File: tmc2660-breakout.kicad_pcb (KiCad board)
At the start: 2 copper layers, 26.9 x 31.1 mm, 25 parts, among them P1 SPI, P2 StepDir, P3 Motor, P4 VCC, P5 VMOT, U1 TMC2660

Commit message: o smallish alignments
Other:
- board text added: "<30V"
- board text added: "I/O"
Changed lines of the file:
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@@
-(kicad_pcb (version 4) (host pcbnew "(2016-01-05 BZR 6425, Git 89c183f)-product")
+(kicad_pcb (version 20160815) (host pcbnew "(2016-10-23 revision 4ee344e)-master")
   (general
     (links 65)
     (no_connects 0)
-    (area 112.74 37.159999 147.476858 73.075952)
+    (area 112.9075 37.159999 156.503832 76.545001)
     (thickness 1.6)
-    (drawings 13)
-    (tracks 333)
+    (drawings 17)
+    (tracks 332)
     (zones 0)
     (modules 25)
@@
       (hpglpenspeed 20)
       (hpglpendiameter 15)
-      (hpglpenoverlay 2)
       (psnegative false)
       (psa4output false)
@@
     (uvia_dia 0.3)
     (uvia_drill 0.1)
+    (diff_pair_gap 0.25)
+    (diff_pair_width 0.2)
     (add_net /BRA)
     (add_net /BRB)
@@
     (tags "resistor 1206")
     (attr smd)
-    (fp_text reference R5 (at 0.039 0 360) (layer F.SilkS)
+    (fp_text reference R5 (at 0.039 0) (layer F.SilkS)
       (effects (font (size 1 1) (thickness 0.15)))
     )
@@
     (tags "capacitor 0805")
     (attr smd)
-    (fp_text reference C1 (at -1.778 -1.778 360) (layer F.SilkS)
+    (fp_text reference C1 (at -1.778 -1.778) (layer F.SilkS)
       (effects (font (size 1 1) (thickness 0.15)))
     )
@@
     (tags "capacitor 0805")
     (attr smd)
-    (fp_text reference C2 (at -1.143 -1.778 360) (layer F.SilkS)
+    (fp_text reference C2 (at -0.999 -1.68) (layer F.SilkS)
       (effects (font (size 1 1) (thickness 0.15)))
     )
@@
     (tags "LED 0805 SMD")
     (attr smd)
-    (fp_text reference D1 (at -2.286 0.635) (layer F.SilkS)
+    (fp_text reference D1 (at -2.621 0.266) (layer F.SilkS)
       (effects (font (size 1 1) (thickness 0.15)))
     )
@@
       (effects (font (size 1 1) (thickness 0.15)))
     )
-    (fp_text value SPI (at -2.54 4.445 360) (layer F.SilkS)
+    (fp_text value SPI (at -2.54 4.445) (layer F.SilkS)
       (effects (font (size 1.5 1.5) (thickness 0.2)))
     )
@@
       (effects (font (size 1 1) (thickness 0.15)))
     )
-    (fp_text value Motor (at -2.54 0.381 360) (layer F.SilkS)
+    (fp_text value Motor (at -2.54 0.381) (layer F.SilkS)
       (effects (font (size 1 1) (thickness 0.15)))
     )
@@
     (tags "resistor 0805")
     (attr smd)
-    (fp_text reference R2 (at -2.54 0.381 360) (layer F.SilkS)
+    (fp_text reference R2 (at -2.54 0.381) (layer F.SilkS)
       (effects (font (size 1 1) (thickness 0.15)))
     )
@@
     (tags "resistor 1206")
     (attr smd)
-    (fp_text reference R4 (at 0.039 0.0635 360) (layer F.SilkS)
+    (fp_text reference R4 (at 0.039 0.0635) (layer F.SilkS)
       (effects (font (size 1 1) (thickness 0.15)))
     )
@@
       (effects (font (size 1 1) (thickness 0.15)) (justify mirror))
     )
-    (fp_text value OSHW (at 4.445 -1.778 540) (layer B.Fab) hide
+    (fp_text value OSHW (at 4.445 -1.778 180) (layer B.Fab) hide
       (effects (font (size 1 1) (thickness 0.15)) (justify mirror))
     )
@@
     (fp_line (start 0.35052 -0.89916) (end 0.7493 -1.89992) (layer B.SilkS) (width 0.15))
   )
-  (module Fiducials:Fiducial_1mm_Dia_2.54mm_Outer_CopperTop (layer F.Cu)
+  (module Fiducials:Fiducial_1mm_Dia_2.54mm_Outer_CopperTop locked (layer F.Cu)
     (at 141.732 38.862)
     (descr "Circular Fiducial, 1mm bare copper top; 2.54mm keepout")
@@
       (solder_mask_margin 0.77) (clearance 0.77))
   )
-  (module Fiducials:Fiducial_1mm_Dia_2.54mm_Outer_CopperTop (layer F.Cu)
+  (module Fiducials:Fiducial_1mm_Dia_2.54mm_Outer_CopperTop locked (layer F.Cu)
     (at 118.11 66.548)
     (descr "Circular Fiducial, 1mm bare copper top; 2.54mm keepout")
@@
     (tags "resistor 2512")
     (attr smd)
-    (fp_text reference R6 (at 1.4605 0.0635 360) (layer F.SilkS)
+    (fp_text reference R6 (at 1.4605 0.0635) (layer F.SilkS)
       (effects (font (size 1 1) (thickness 0.15)))
     )
@@
     (tags "resistor 2512")
     (attr smd)
-    (fp_text reference R7 (at 1.5875 0 360) (layer F.SilkS)
-      (effects (font (size 1 1) (thickness 0.15)))
-    )
-    (fp_text value 0.075 (at -1.4605 -6.731 450) (layer F.Fab)
+    (fp_text reference R7 (at 1.5875 0) (layer F.SilkS)
+      (effects (font (size 1 1) (thickness 0.15)))
+    )
+    (fp_text value 0.075 (at -1.4605 -6.731 90) (layer F.Fab)
       (effects (font (size 1 1) (thickness 0.15)))
     )
@@
     (tags "capacitor 0805")
     (attr smd)
-    (fp_text reference C8 (at -0.889 -2.413 360) (layer F.SilkS)
-      (effects (font (size 1 1) (thickness 0.15)))
-    )
-    (fp_text value 10n (at 4.826 0 450) (layer F.Fab)
+    (fp_text reference C8 (at -0.889 -2.413) (layer F.SilkS)
+      (effects (font (size 1 1) (thickness 0.15)))
+    )
+    (fp_text value 10n (at 4.826 0 90) (layer F.Fab)
       (effects (font (size 1 1) (thickness 0.15)))
     )
@@
       (rotate (xyz 0 0 0))
     )
+  )
+  (dimension 27 (width 0.3) (layer Eco1.User)
+    (gr_text "27.000 mm" (at 129.5 75.15) (layer Eco1.User)
+      (effects (font (size 1.5 1.5) (thickness 0.3)))
+    )
+    (feature1 (pts (xy 143 69) (xy 143 76.5)))
+    (feature2 (pts (xy 116 69) (xy 116 76.5)))
+    (crossbar (pts (xy 116 73.8) (xy 143 73.8)))
+    (arrow1a (pts (xy 143 73.8) (xy 141.873496 74.386421)))
+    (arrow1b (pts (xy 143 73.8) (xy 141.873496 73.213579)))
+    (arrow2a (pts (xy 116 73.8) (xy 117.126504 74.386421)))
+    (arrow2b (pts (xy 116 73.8) (xy 117.126504 73.213579)))
+  )
+  (dimension 31.1 (width 0.3) (layer Eco1.User)
+    (gr_text "31.100 mm" (at 149.853831 53.15 270) (layer Eco1.User)
+      (effects (font (size 1.5 1.5) (thickness 0.3)))
+    )
+    (feature1 (pts (xy 143.3 68.7) (xy 151.203831 68.7)))
+    (feature2 (pts (xy 143.3 37.6) (xy 151.203831 37.6)))
+    (crossbar (pts (xy 148.503831 37.6) (xy 148.503831 68.7)))
+    (arrow1a (pts (xy 148.503831 68.7) (xy 147.91741 67.573496)))
+    (arrow1b (pts (xy 148.503831 68.7) (xy 149.090252 67.573496)))
+    (arrow2a (pts (xy 148.503831 37.6) (xy 147.91741 38.726504)))
+    (arrow2b (pts (xy 148.503831 37.6) (xy 149.090252 38.726504)))
+  )
+  (gr_text I/O (at 120.777 41.402) (layer F.SilkS)
+    (effects (font (size 0.8 0.8) (thickness 0.15)) (justify left))
+  )
+  (gr_text <30V (at 138.811 43.053) (layer F.SilkS)
+    (effects (font (size 0.8 0.8) (thickness 0.15)) (justify right))
   )
   (gr_text "github.com\nhzeller/tmc2660-breakout" (at 135.128 41.402 90) (layer B.SilkS)
@@
   (segment (start 124.696602 64.786) (end 123.571 64.786) (width 0.4) (layer F.Cu) (net 4))
   (segment (start 126.6575 60.206) (end 126.6575 62.825102) (width 0.4) (layer F.Cu) (net 4))
-  (segment (start 122.2375 52.756) (end 121.464 52.756) (width 0.5) (layer F.Cu) (net 5))
-  (segment (start 124.0075 52.756) (end 122.2375 52.756) (width 0.5) (layer F.Cu) (net 5))
-  (segment (start 122.2375 52.756) (end 122.4915 52.756) (width 0.25) (layer F.Cu) (net 5))
+  (segment (start 122.67625 52.756) (end 121.90275 52.756) (width 1) (layer F.Cu) (net 5))
+  (segment (start 124.0075 52.756) (end 122.2375 52.756) (width 0.6) (layer F.Cu) (net 5))
   (segment (start 121.464 52.756) (end 121.388 52.832) (width 0.25) (layer F.Cu) (net 5))
-  (segment (start 125.7425 52.756) (end 124.0075 52.756) (width 0.5) (layer F.Cu) (net 5))
-  (segment (start 129.362 52.756) (end 125.7425 52.756) (width 1) (layer F.Cu) (net 5))
+  (segment (start 125.7425 52.756) (end 124.0075 52.756) (width 0.6) (layer F.Cu) (net 5))
+  (segment (start 129.3495 52.756) (end 125.73 52.756) (width 1) (layer F.Cu) (net 5))
   (segment (start 129.362 52.756) (end 132.2575 49.8605) (width 1) (layer F.Cu) (net 5))
   (segment (start 132.2575 49.8605) (end 132.2575 48.506) (width 0.25) (layer F.Cu) (net 5))
@@
       (pts
         (xy 118.872 53.34) (xy 124.714 53.34) (xy 124.714 54.61) (xy 122.682 54.61) (xy 122.682 55.6895)
-        (xy 118.999 55.6895) (xy 118.999 57.404) (xy 124.714 57.404) (xy 124.714 58.674) (xy 118.872 58.674)
+        (xy 118.999 55.6895) (xy 118.999 57.277) (xy 124.714 57.277) (xy 124.714 58.674) (xy 118.872 58.674)
       )
     )

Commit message: o Label some previously anonymous nets (e.g. Step/Dir).
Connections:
- net Net-(C6-Pad1) renamed VCC
- net Net-(P1-Pad1) renamed /~CS
- net Net-(P1-Pad2) renamed /SCLK
- net Net-(P1-Pad3) renamed /MOSI
- net Net-(P1-Pad4) renamed /MISO
- net Net-(P2-Pad1) renamed /DIR
- net Net-(P2-Pad2) renamed /STEP

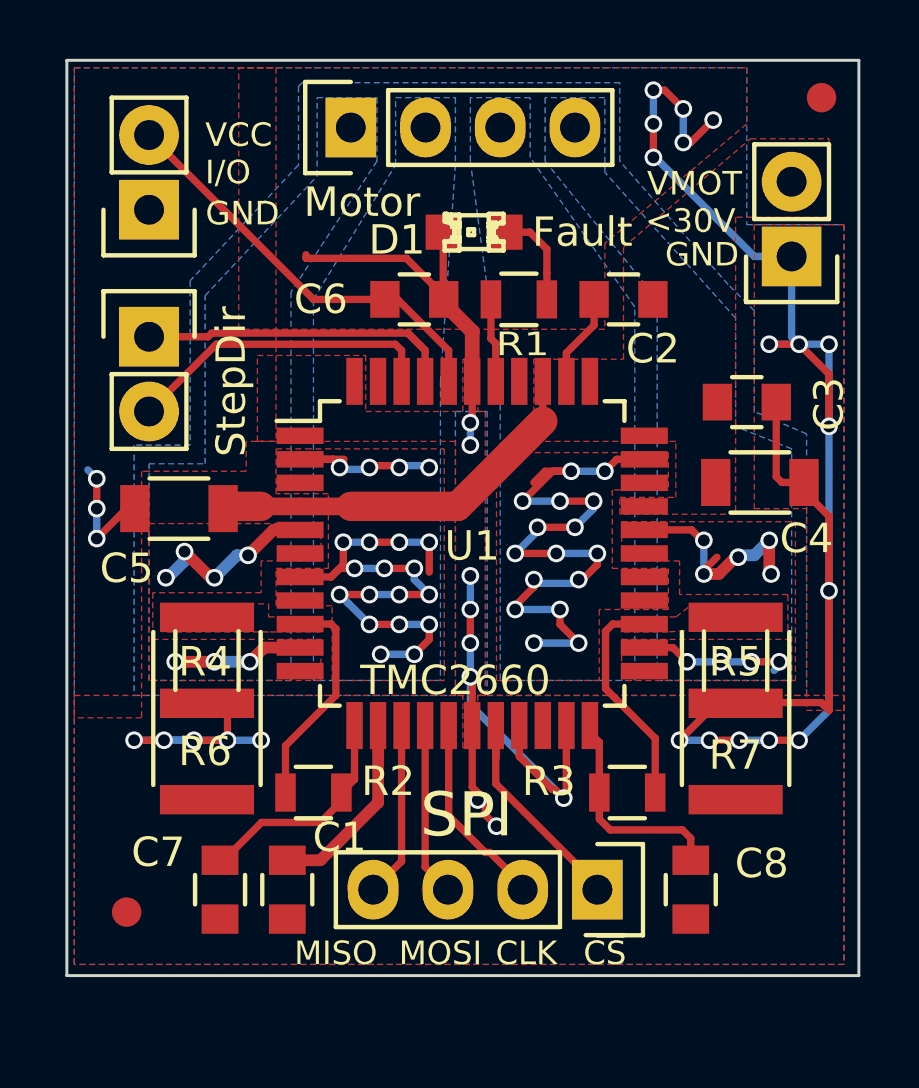
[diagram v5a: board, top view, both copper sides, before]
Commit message: Use current KiCAD 5.x libraries.
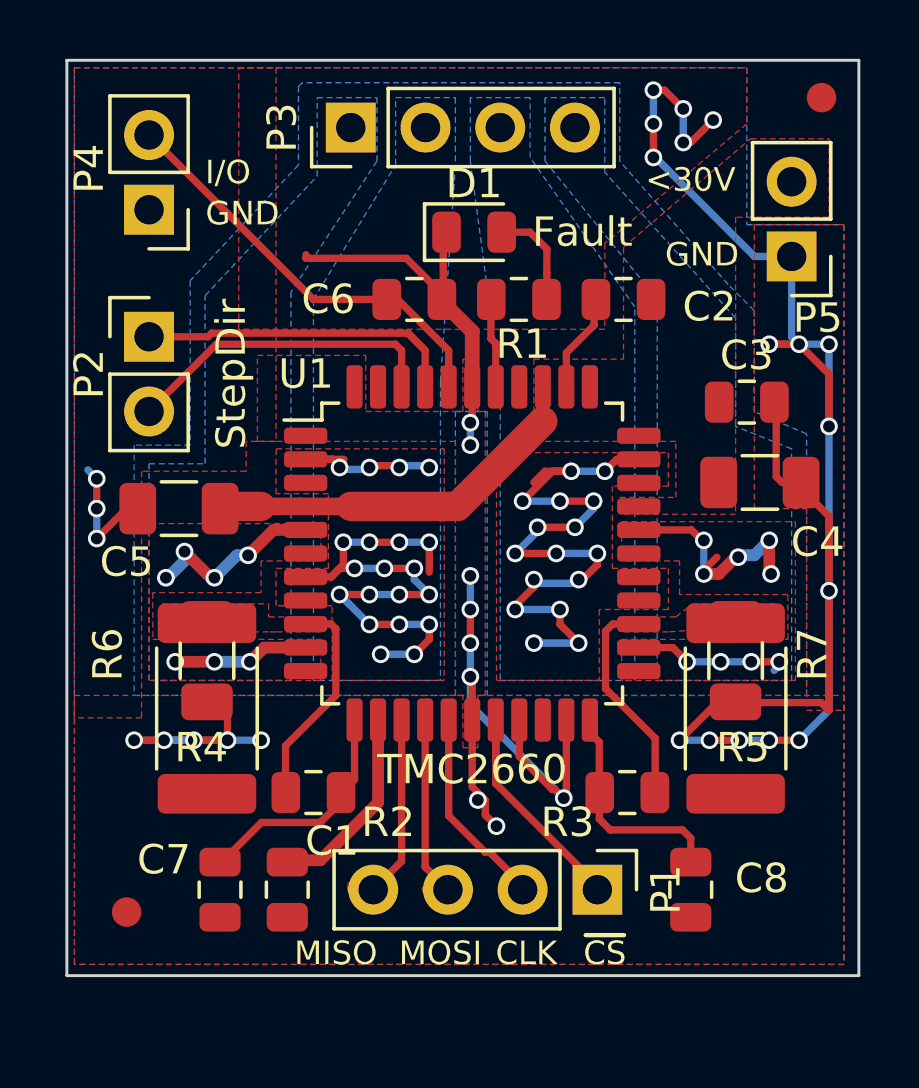
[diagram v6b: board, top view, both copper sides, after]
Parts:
- C1, C2, C3, C6, C7, C8: footprint Capacitors_SMD:C_0805 -> Capacitor_SMD:C_0805_2012Metric
- C4, C5: footprint Capacitors_SMD:C_1206 -> Capacitor_SMD:C_1206_3216Metric
- D1: footprint LEDs:LED-0805 -> LED_SMD:LED_0805_2012Metric
- P1, P3: footprint Pin_Headers:Pin_Header_Straight_1x04 -> Connector_PinHeader_2.54mm:PinHeader_1x04_P2.54mm_Vertical
- P2, P4, P5: footprint Pin_Headers:Pin_Header_Straight_1x02 -> Connector_PinHeader_2.54mm:PinHeader_1x02_P2.54mm_Vertical
- R1, R2, R3: footprint Resistors_SMD:R_0805 -> Resistor_SMD:R_0805_2012Metric
- R4, R5: footprint Resistors_SMD:R_1206 -> Resistor_SMD:R_1206_3216Metric
- R6, R7: footprint Resistors_SMD:R_2512 -> Resistor_SMD:R_2512_6332Metric
- U1: footprint Housings_QFP:LQFP-44_10x10mm_Pitch0.8mm -> Package_QFP:LQFP-44_10x10mm_P0.8mm
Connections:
- U1 pad 43: (no net) -> Net-(U1-Pad43)
